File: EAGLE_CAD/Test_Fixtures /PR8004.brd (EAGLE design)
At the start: 100 x 91 mm, 43 parts, among them J1 M3_SCREW_POST

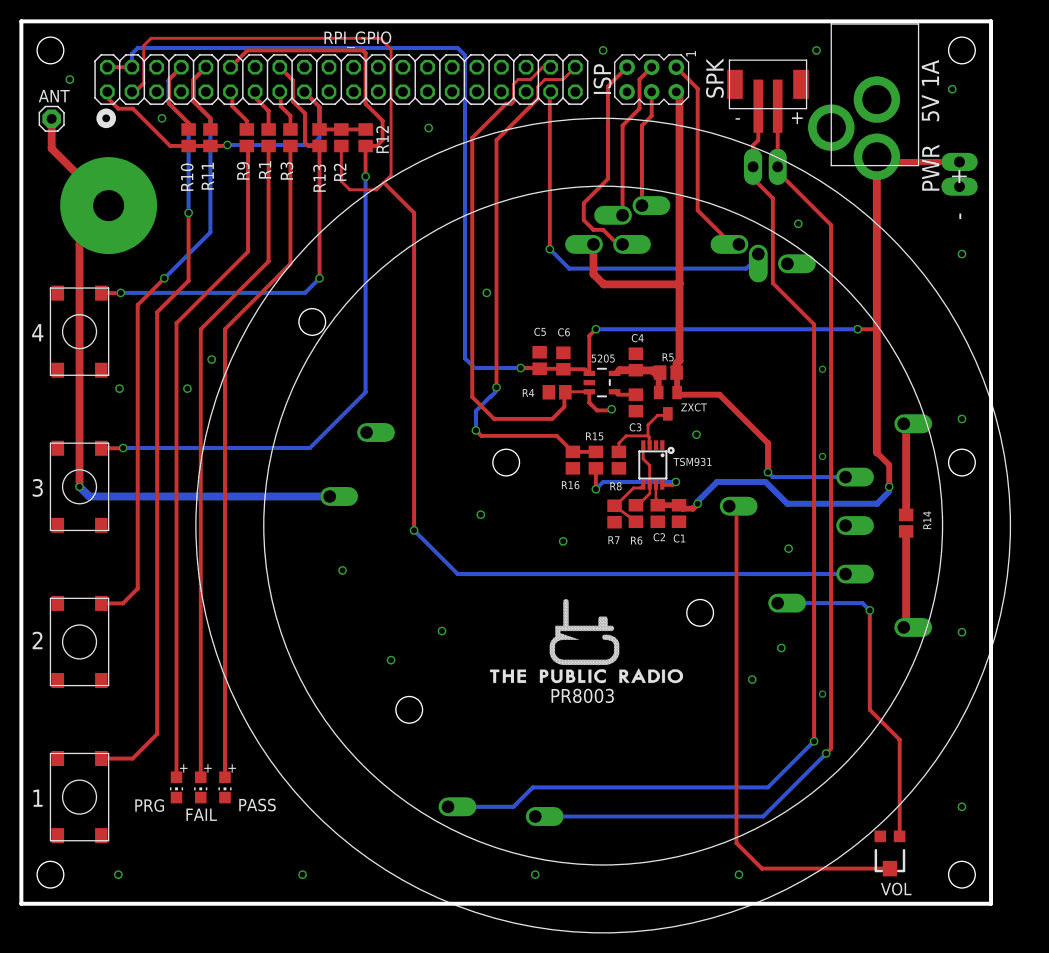
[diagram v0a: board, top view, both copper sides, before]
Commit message: Pushed to PR8003 Test Fixture
Updated layout on headers and orientation.
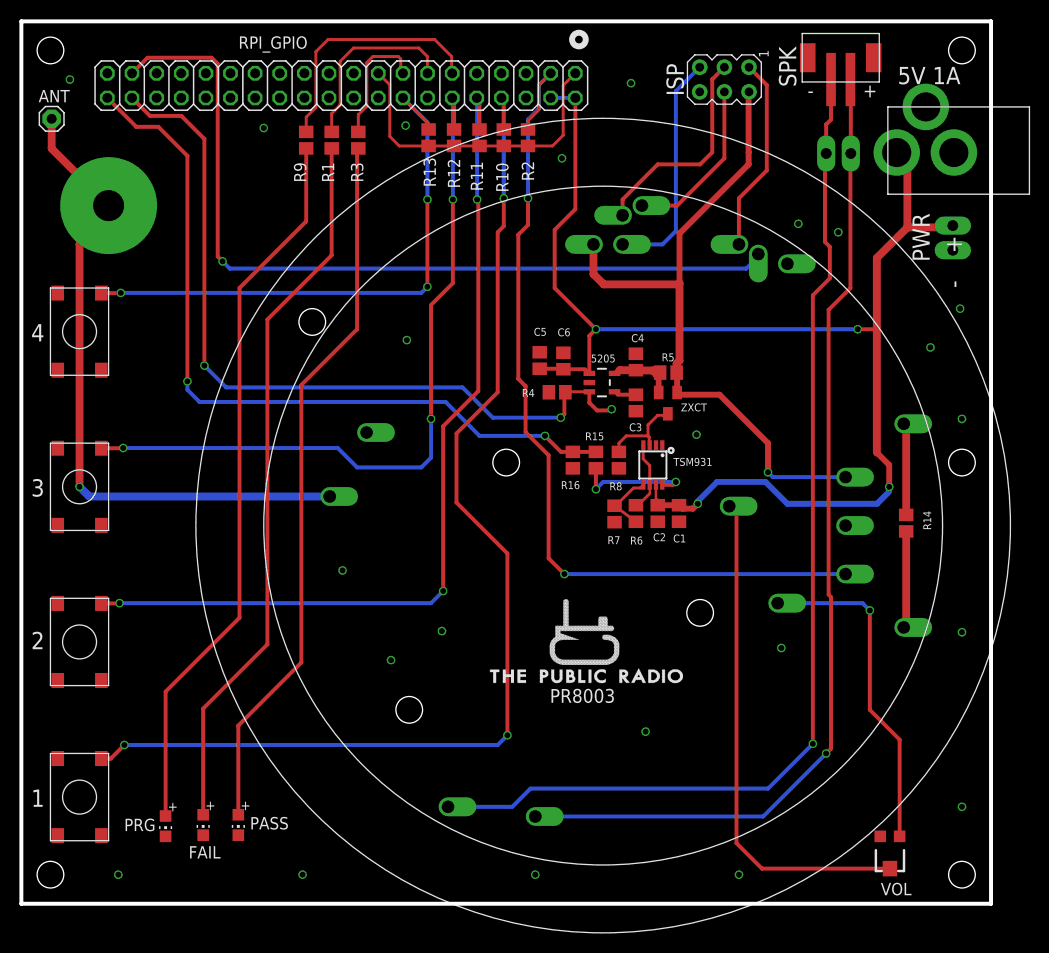
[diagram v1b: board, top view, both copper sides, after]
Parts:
- moved R10 32.5 mm to (49.8, 79.0)
- moved R11 27.8 mm to (47.2, 79.0)
- moved R2 19.2 mm to (52.2, 79.0), turned to 90 degrees
- moved U$19 14.4 mm to (99.6, 77.6), turned to 270 degrees
- moved R13 11.2 mm to (42.0, 79.0), turned to 90 degrees
- moved R12 9.12 mm to (44.6, 79.0), turned to 90 degrees
- moved CN1 7.99 mm to (84.5, 87.8)
- moved ISP 7.50 mm to (72.5, 85.0)
- moved R3 7.00 mm to (34.8, 78.8)
- moved JP3 6.60 mm to (96.1, 69.9)
- moved R1 6.50 mm to (32.0, 78.8)
- moved R9 6.13 mm to (29.4, 78.8)
- moved JP2 5.19 mm to (83.0, 77.4), turned to 0 degrees
- moved PRG 4.16 mm to (14.9, 8.00)
- moved PASS 4.11 mm to (22.4, 8.12)
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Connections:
- net SPK_OUT+: now also JP2.1; no longer JP2.2
- net SPK_OUT-: now also JP2.2; no longer JP2.1
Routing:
- net +5V: track 190.1 -> 140.4 mm, vias 5 -> 4
- net TACSW: track 39.4 -> 86.7 mm
- net DEV_PRES: track 138.0 -> 90.8 mm, vias 1 -> 2
- net TAC1: track 86.1 -> 116.2 mm, vias 1 -> 3
- net COMPARATOR: track 56.1 -> 79.6 mm
- net REG_ENABLE: track 57.7 -> 80.7 mm, vias 1 -> 3
- net TAC2: track 70.2 -> 91.6 mm, vias 1 -> 3
- net PROCESS: track 4.58 -> 25.7 mm
- net FAIL: track 4.46 -> 19.3 mm
- net TAC4: track 47.3 -> 58.8 mm, vias 2 -> 3
- net PASS: track 4.34 -> 12.9 mm
- net +3V3: track 39.5 -> 32.7 mm, vias 1 -> 0
- net N$2: track 68.2 -> 74.9 mm
- net N$3: track 68.0 -> 74.2 mm
- net N$4: track 67.9 -> 73.9 mm
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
